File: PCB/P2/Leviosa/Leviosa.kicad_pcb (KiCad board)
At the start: 2 copper layers, 80 x 80 mm, 52 parts, among them J1 2.54mm 1x03 Servo 1, J2 2.54mm 1x03 Servo 1, J3 2.54mm 1x03 Spare, J4 Barrel_Jack, Q3 TIP122, Q4 TIP122, U1 LM324, U2 ATtiny13A-P, U3 TPS1H200AQDGNRQ1, U5 L7805, U6 SS495A

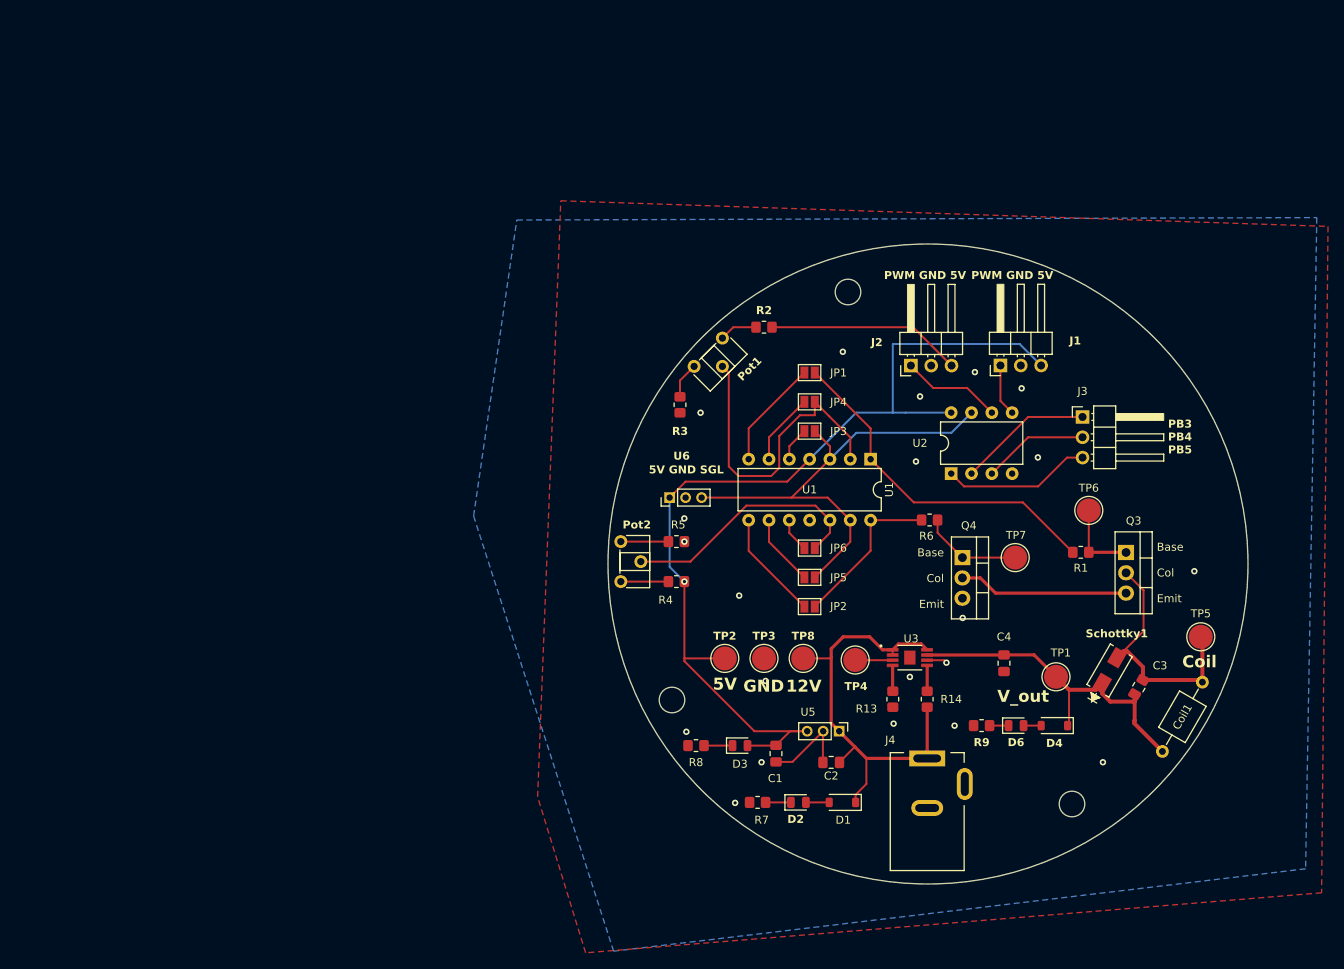
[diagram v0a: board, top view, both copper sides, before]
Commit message: PCB P2 review (#18)
* update some PCB components as part of P2 iteration

* swap components, add start of current sense circuit

* flesh out schematic

* add datasheets

* fix inputs to current sense

* Moved some stuff around for clarity/good formating. Added some To Doos on the .txt

* Fixed current sense input

* update file with some values for current sensing circuit

* update schematic

* update footprints, start pcb

* update node naming & PCB

* update PCB

* finish initial pcb layout

* update a resistor and PCB

* update a resistor footprint

* Update schematic layout for clarity

* move 5V TP

* added cap to attiny and fixed resistors to 8.2R

* update schematic and pcb per Jack's feedback

* update PCB

pending trace width update potentially (long 5V and 12Vout)

* update pcb

* add fiducials and add thickness to 5V

* add test images (various)

---------

Co-authored-by: AirMatress <bluemoonjack8@gmail.com>
Co-authored-by: Daniel <135270549+danielMosaic@users.noreply.github.com>
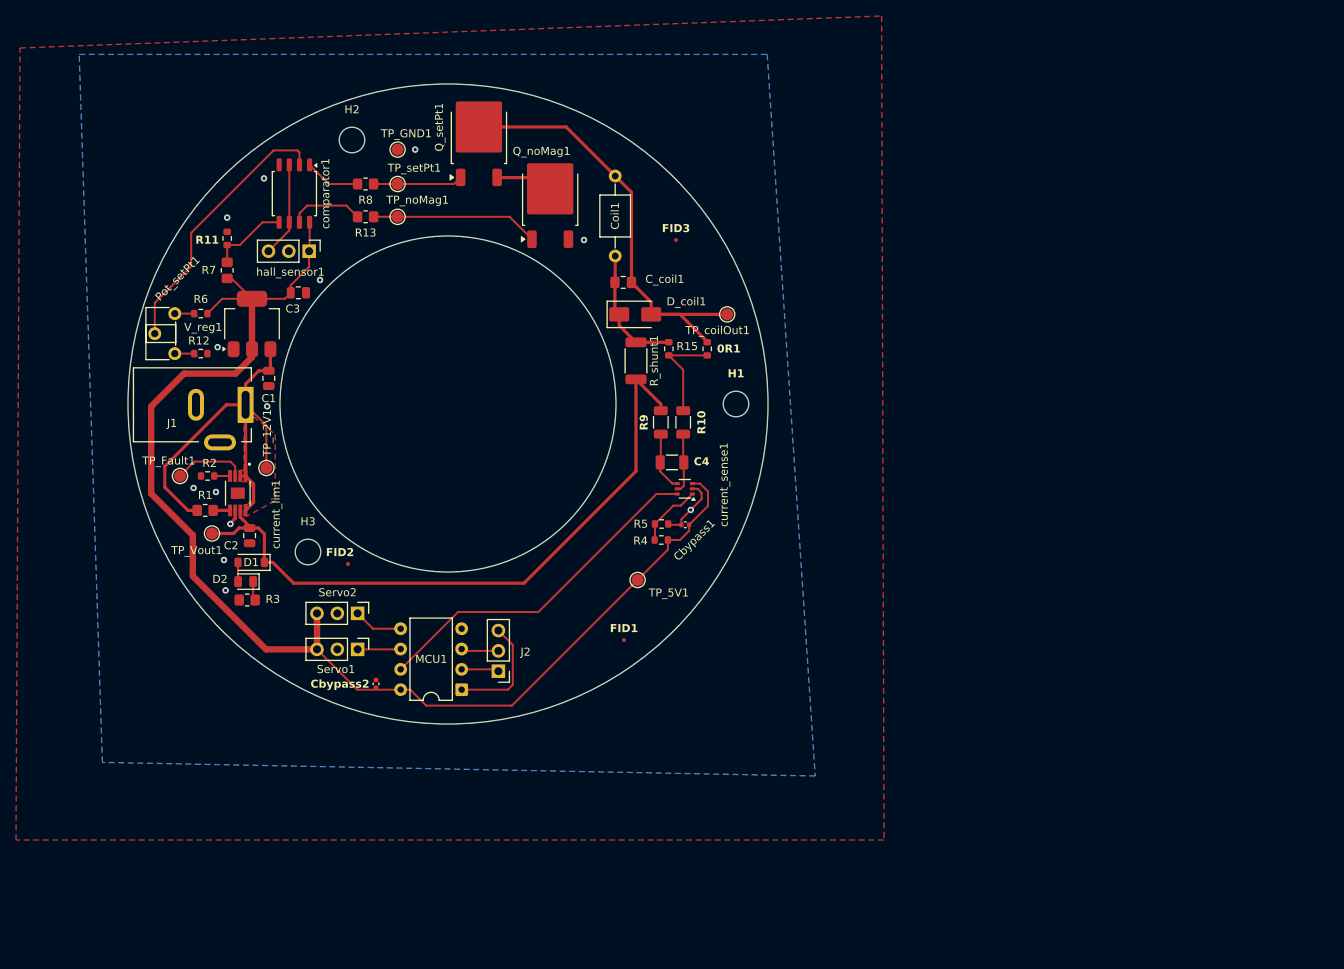
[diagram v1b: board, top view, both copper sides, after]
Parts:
- removed D3, D6: LED, LED_SMD:LED_0805_2012Metric
- removed D4: BZT52C8V2 WD, Diode_SMD:D_SOD-123
- removed J3: 2.54mm 1x03 Spare, Connector_PinHeader_2.54mm:PinHeader_1x03_P2.54mm_Horizontal
- removed J4: Barrel_Jack, Connector_BarrelJack:BarrelJack_Kycon_KLDX-0202-xC_Horizontal
- removed JP1, JP2, JP3, JP4, JP5, JP6: SolderJumper_2_Open, Jumper:SolderJumper-2_P1.3mm_Open_Pad1.0x1.5mm
- removed Pot1, Pot2: 3362S-1-103LF, Potentiometer_THT:Potentiometer_ACP_CA6-H2,5_Horizontal
- removed Q3, Q4: TIP122, Package_TO_SOT_THT:TO-220-3_Vertical
- removed R14: 100kΩ, Resistor_SMD:R_0805_2012Metric_Pad1.20x1.40mm_HandSolder
- removed Schottky1: Schottky Diode SR206-TPCT-ND1, B230A_13_F:SMA_DIO
- removed TP1: Vout, TestPoint:TestPoint_Pad_D3.0mm
- removed TP2: 5V, TestPoint:TestPoint_Pad_D3.0mm
- removed TP3: GND, TestPoint:TestPoint_Pad_D3.0mm
- removed TP4: Fault, TestPoint:TestPoint_Pad_D3.0mm
- removed TP5: coil_out, TestPoint:TestPoint_Pad_D3.0mm
- removed TP6: set_point_trigger, TestPoint:TestPoint_Pad_D3.0mm
- removed TP7: no_magnet_point_trigger, TestPoint:TestPoint_Pad_D3.0mm
- removed TP8: 12V, TestPoint:TestPoint_Pad_D3.0mm
- removed U1: LM324, Package_DIP:DIP-14_W7.62mm
- removed U2: ATtiny13A-P, Package_DIP:DIP-8_W7.62mm
- removed U3: TPS1H200AQDGNRQ1, TPS1H200AQDGNRQ1:SOP65P490X110-9N
- removed U5: L7805, Connector_PinHeader_2.00mm:PinHeader_1x03_P2.00mm_Vertical
- removed U6: SS495A, Connector_PinHeader_2.00mm:PinHeader_1x03_P2.00mm_Vertical
- added 0R1: DNP, Resistor_SMD:R_0603_1608Metric, F.Cu at (132.4, 93.1)
- added C_coil1: 20nF, Capacitor_SMD:C_0805_2012Metric_Pad1.18x1.45mm_HandSolder, F.Cu at (121.9, 84.8)
- added Cbypass1: 0.1µF, Capacitor_SMD:C_0402_1005Metric, F.Cu at (129.7, 115.1)
- added Cbypass2: 0.1µF, Capacitor_SMD:C_0402_1005Metric, F.Cu at (91.0, 135.0)
- added D_coil1: SS34, Diode_SMD:D_SMA, F.Cu at (123.4, 88.8)
- added FID1: Fiducial, Fiducial:Fiducial_0.5mm_Mask1mm, F.Cu at (122.0, 129.5)
- added FID2: Fiducial, Fiducial:Fiducial_0.5mm_Mask1mm, F.Cu at (87.5, 120.0)
- added FID3: Fiducial, Fiducial:Fiducial_0.5mm_Mask1mm, F.Cu at (128.5, 79.5)
- added MCU1: ATtiny13A-P, Package_DIP:DIP-8_W7.62mm, F.Cu at (101.7, 135.7)
- added Pot_setPt1: 3362S-1-103LF, Potentiometer_THT:Potentiometer_ACP_CA6-H2,5_Horizontal, F.Cu at (65.8, 93.7)
- added Q_noMag1: NCE0110K, Package_TO_SOT_SMD:TO-252-2, F.Cu at (112.8, 74.4)
- added Q_setPt1: NCE0110K, Package_TO_SOT_SMD:TO-252-2, F.Cu at (103.9, 66.6)
- added R10: 8.2Ω, Resistor_SMD:R_1206_3216Metric, F.Cu at (129.4, 102.3)
- added R11: 68kΩ, Resistor_SMD:R_0603_1608Metric, F.Cu at (72.4, 79.3)
- added R12: 3.9kΩ, Resistor_SMD:R_0603_1608Metric, F.Cu at (69.1, 93.7)
- added R15: 0Ω, Resistor_SMD:R_0603_1608Metric, F.Cu at (127.6, 93.1)
- added R_shunt1: 50mΩ, Resistor_SMD:R_2010_5025Metric, F.Cu at (123.5, 94.6)
- added Servo1: 2.54mm 1x03 Servo 1, Connector_PinHeader_2.54mm:PinHeader_1x03_P2.54mm_Vertical, F.Cu at (88.7, 130.7)
- added Servo2: 2.54mm 1x03 Servo 1, Connector_PinHeader_2.54mm:PinHeader_1x03_P2.54mm_Vertical, F.Cu at (88.7, 126.2)
- added TP_12V1: 12V, TestPoint:TestPoint_Pad_D1.5mm, F.Cu at (77.3, 108.0)
- added TP_5V1: 5V, TestPoint:TestPoint_Pad_D1.5mm, F.Cu at (123.7, 122.0)
- added TP_Fault1: Fault, TestPoint:TestPoint_Pad_D1.5mm, F.Cu at (66.5, 109.0)
- added TP_GND1: GND, TestPoint:TestPoint_Pad_D1.5mm, F.Cu at (93.7, 68.2)
- added TP_Vout1: Vout, TestPoint:TestPoint_Pad_D1.5mm, F.Cu at (70.5, 116.2)
- added TP_coilOut1: coil_out, TestPoint:TestPoint_Pad_D1.5mm, F.Cu at (134.9, 88.8)
- added TP_noMag1: no_magnet_point_trigger, TestPoint:TestPoint_Pad_D1.5mm, F.Cu at (93.7, 76.6)
- added TP_setPt1: set_point_trigger, TestPoint:TestPoint_Pad_D1.5mm, F.Cu at (93.7, 72.5)
- added V_reg1: AMS1117-5.0, Package_TO_SOT_SMD:SOT-223-3_TabPin2, F.Cu at (75.5, 90.0)
- added comparator1: LM393, Package_SO:SOIC-8_5.3x5.3mm_P1.27mm, F.Cu at (80.8, 73.7)
- added current_lim1: TPS1H200AQDGNRQ1, TPS1H200AQDGNRQ1:SOP65P490X110-9N, F.Cu at (73.7, 111.2)
- added current_sense1: INA199xxDCK (50V/V), Package_TO_SOT_SMD:SOT-363_SC-70-6, F.Cu at (129.6, 110.6)
- added hall_sensor1: SS495A, Connector_PinHeader_2.54mm:PinHeader_1x03_P2.54mm_Vertical, F.Cu at (82.6, 80.9)
- C1: value 0.1µF -> 22µF; footprint Capacitor_SMD:C_0805_2012Metric_Pad1.18x1.45mm_HandSolder -> Capacitor_SMD:C_0805_2012Metric
- C2: value 0.33µF -> 22µF; footprint Capacitor_SMD:C_0805_2012Metric_Pad1.18x1.45mm_HandSolder -> Capacitor_SMD:C_0805_2012Metric
- C3: value 20nF -> 22µF; footprint Capacitor_SMD:C_0805_2012Metric_Pad1.18x1.45mm_HandSolder -> Capacitor_SMD:C_0805_2012Metric
- C4: value 10µF -> 47μF; footprint Capacitor_SMD:C_0805_2012Metric_Pad1.18x1.45mm_HandSolder -> Capacitor_SMD:C_1206_3216Metric
- J1: value 2.54mm 1x03 Servo 1 -> Barrel_Jack; footprint Connector_PinHeader_2.54mm:PinHeader_1x03_P2.54mm_Horizontal -> Connector_BarrelJack:BarrelJack_Kycon_KLDX-0202-xC_Horizontal
- J2: value 2.54mm 1x03 Servo 1 -> 2.54mm 1x03 Spare; footprint Connector_PinHeader_2.54mm:PinHeader_1x03_P2.54mm_Horizontal -> Connector_PinHeader_2.54mm:PinHeader_1x03_P2.54mm_Vertical
- R1, R7: value 1kΩ -> 100kΩ
- R13: value 8kΩ -> 1kΩ
- R2: value 100kΩ -> 3.9kΩ; footprint Resistor_SMD:R_0805_2012Metric_Pad1.20x1.40mm_HandSolder -> Resistor_SMD:R_0603_1608Metric
- R3: value 7.8kΩ -> 1kΩ
- R4: value 100kΩ -> DNP; footprint Resistor_SMD:R_0805_2012Metric_Pad1.20x1.40mm_HandSolder -> Resistor_SMD:R_0603_1608Metric
- R5: value 54.2kΩ -> 0Ω; footprint Resistor_SMD:R_0805_2012Metric_Pad1.20x1.40mm_HandSolder -> Resistor_SMD:R_0603_1608Metric
- R6: value 1kΩ -> 51kΩ; footprint Resistor_SMD:R_0805_2012Metric_Pad1.20x1.40mm_HandSolder -> Resistor_SMD:R_0603_1608Metric
- R8: value 400 -> 1kΩ
- R9: value 1kΩ -> 8.2Ω; footprint Resistor_SMD:R_0805_2012Metric_Pad1.20x1.40mm_HandSolder -> Resistor_SMD:R_1206_3216Metric
- moved C3 116.0 mm to (81.3, 86.1), turned to 0 degrees
- moved R1 109.6 mm to (69.7, 113.3)
- moved H3 100.6 mm to (82.5, 118.5)
- moved R6 94.7 mm to (69.1, 88.7), turned to 0 degrees
- moved J1 94.5 mm to (74.7, 100.1), turned to 0 degrees
- moved R7 93.9 mm to (72.4, 83.3), turned to -90 degrees
- moved Coil1 92.3 mm to (120.9, 81.5), turned to 90 degrees
- moved R13 89.3 mm to (89.7, 76.6), turned to 180 degrees
- moved R8 81.4 mm to (89.7, 72.5)
- moved H2 80.6 mm to (88.0, 67.0)
- moved D1 79.8 mm to (75.4, 119.8)
- moved C1 78.9 mm to (77.6, 96.8)
- moved C2 78.0 mm to (75.2, 116.5), turned to -90 degrees
- moved D2 74.4 mm to (74.7, 122.2), turned to 180 degrees
- moved R2 72.0 mm to (70.0, 109.0)
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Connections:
- C1 pad 1: /5V -> +12V
- C2 pad 1: +12V -> /V_out
- C3 pad 1: /V_out -> /5V
- C3 pad 2: /coil_output -> GND
- C4 pad 1: /V_out -> Net-(current_sense1-+)
- C4 pad 2: GND -> Net-(current_sense1--)
- Coil1 pad 1: /V_out -> Net-(D_coil1-K)
- D1 pad 1: +12V -> /V_out
- J1 pad 1: /servo2_control -> +12V
- J1 pad 3: /5V -> (no net)
- J2 pad 1: /servo1_control -> /PB3
- J2 pad 2: GND -> /PB4
- J2 pad 3: /5V -> /PB5
- R1 pad 2: /set_point_trigger -> +12V
- R13 pad 1: GND -> Net-(Q_noMag1-G)
- R13 pad 2: Net-(U3-CL) -> /no_magnet_point_trigger
- R2 pad 1: Net-(Pot1-Pad1) -> GND
- R2 pad 2: /5V -> Net-(current_lim1-CL)
- R3 pad 1: GND -> Net-(D2-K)
- R3 pad 2: Net-(Pot1-Pad3) -> GND
- R4 pad 1: Net-(Pot2-Pad3) -> Net-(current_sense1-REF)
- R5 pad 2: Net-(Pot2-Pad1) -> Net-(current_sense1-REF)
- R6 pad 2: /no_magnet_point_trigger -> /5V
- R7 pad 1: Net-(D2-K) -> /no_magnet_point
- R7 pad 2: GND -> /5V
- R8 pad 2: GND -> /set_point_trigger
- R9 pad 1: Net-(D6-K) -> /V_out
- R9 pad 2: GND -> Net-(current_sense1-+)
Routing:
- net /PB2: track 59.9 -> 0.00 mm
- net /current_sense: track 0.00 -> 43.6 mm
- net /V_out: track 43.0 -> 83.5 mm
- net /set_point_trigger: track 43.8 -> 6.98 mm
- net /coil_output: track 32.2 -> 56.6 mm
- net /no_magnet_point: track 31.6 -> 9.85 mm
- net Net-(Q_noMag1-G): track 0.00 -> 21.0 mm
- net Net-(D_coil1-K): track 0.00 -> 16.0 mm
- net /transistor1_output: track 21.2 -> 7.22 mm
- net /spare_set_point_trigger: track 13.7 -> 0.00 mm
- net /spare_no_magnet_point_trigger: track 13.7 -> 0.00 mm
- net /5V: track 149.5 -> 162.5 mm, vias 1 -> 0
- net Net-(0R1-Pad1): track 0.00 -> 12.5 mm
- net /PB3: track 16.8 -> 4.69 mm
- net /hall_output: track 0.00 -> 11.9 mm
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- added copper zone on F.Cu, net +12V
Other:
- outline, holes or cut-outs redrawn
- board text removed: "12V"
- board text removed: "5V"
- board text removed: "5V GND SGL"
- board text removed: "Base Col Emit"
- board text removed: "Coil"
- board text removed: "GND"
- board text removed: "PB3 PB4 PB5"
- board text removed: "PWM GND 5V"
- board text removed: "V_out"
